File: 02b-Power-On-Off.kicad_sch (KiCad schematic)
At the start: 13 parts, among them Q1 DMG2305UX-7, Q2 DMG2305UX-7, Q4 BSS138, SW5 SW_Push

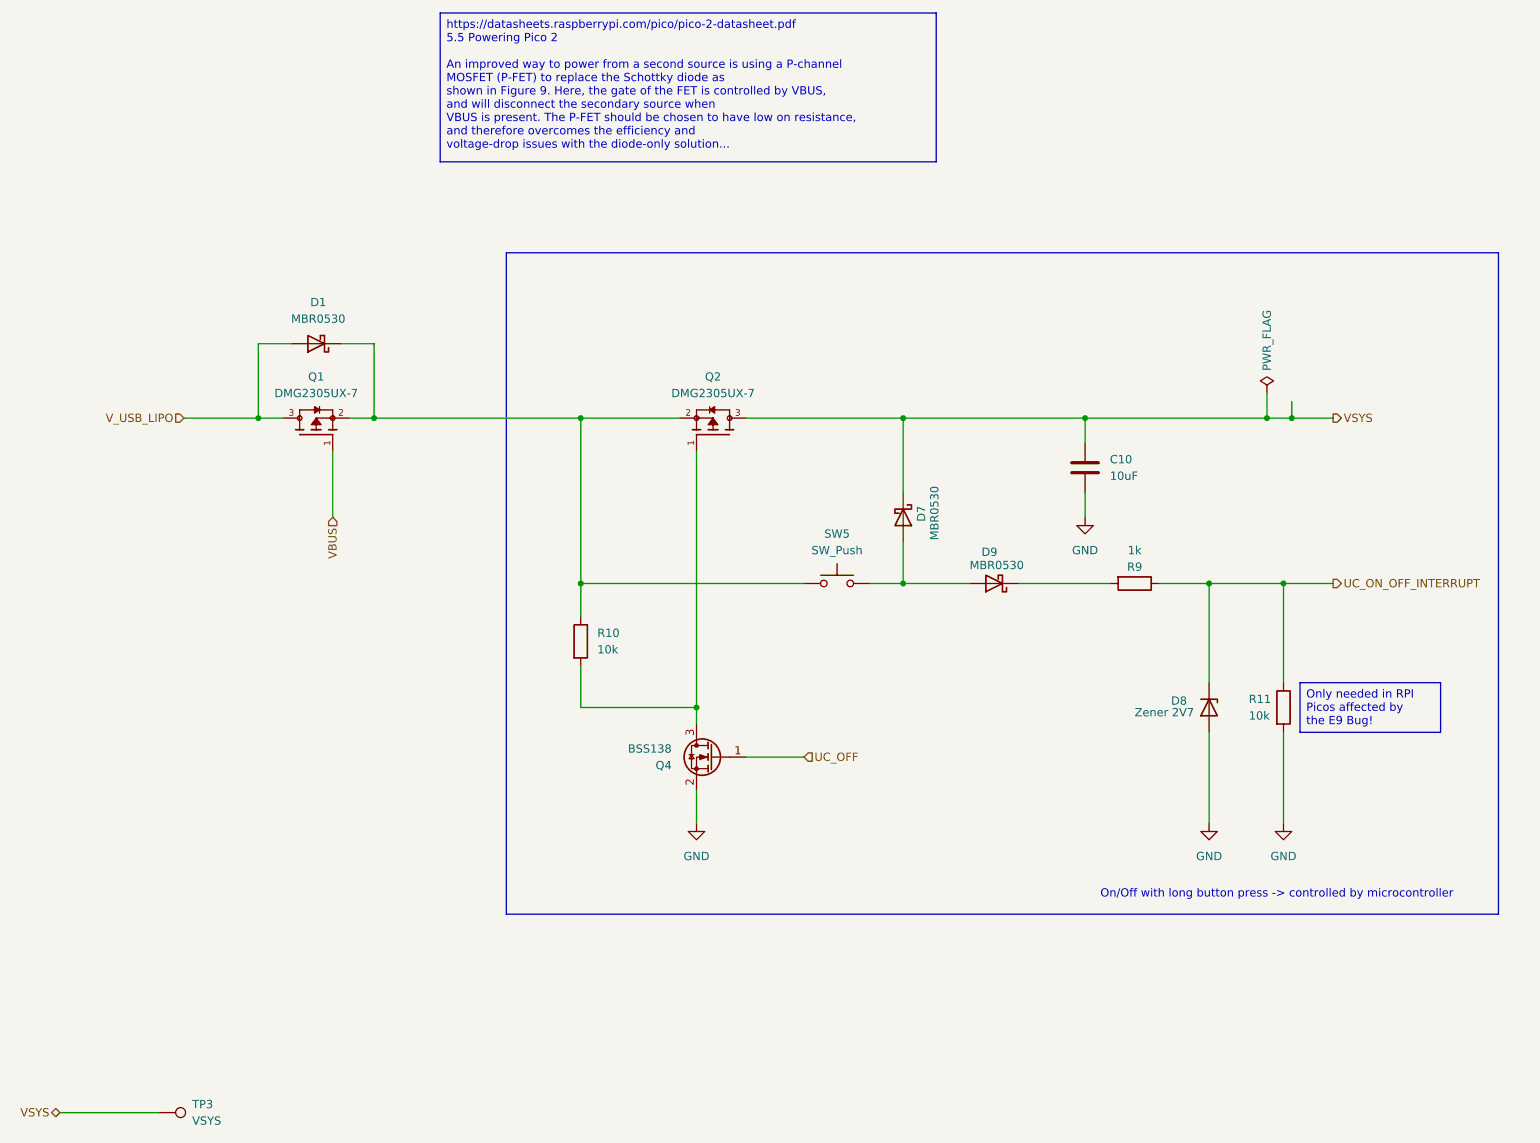
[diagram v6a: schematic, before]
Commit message: Connect both USB data lines again, checked everything with datasheets again
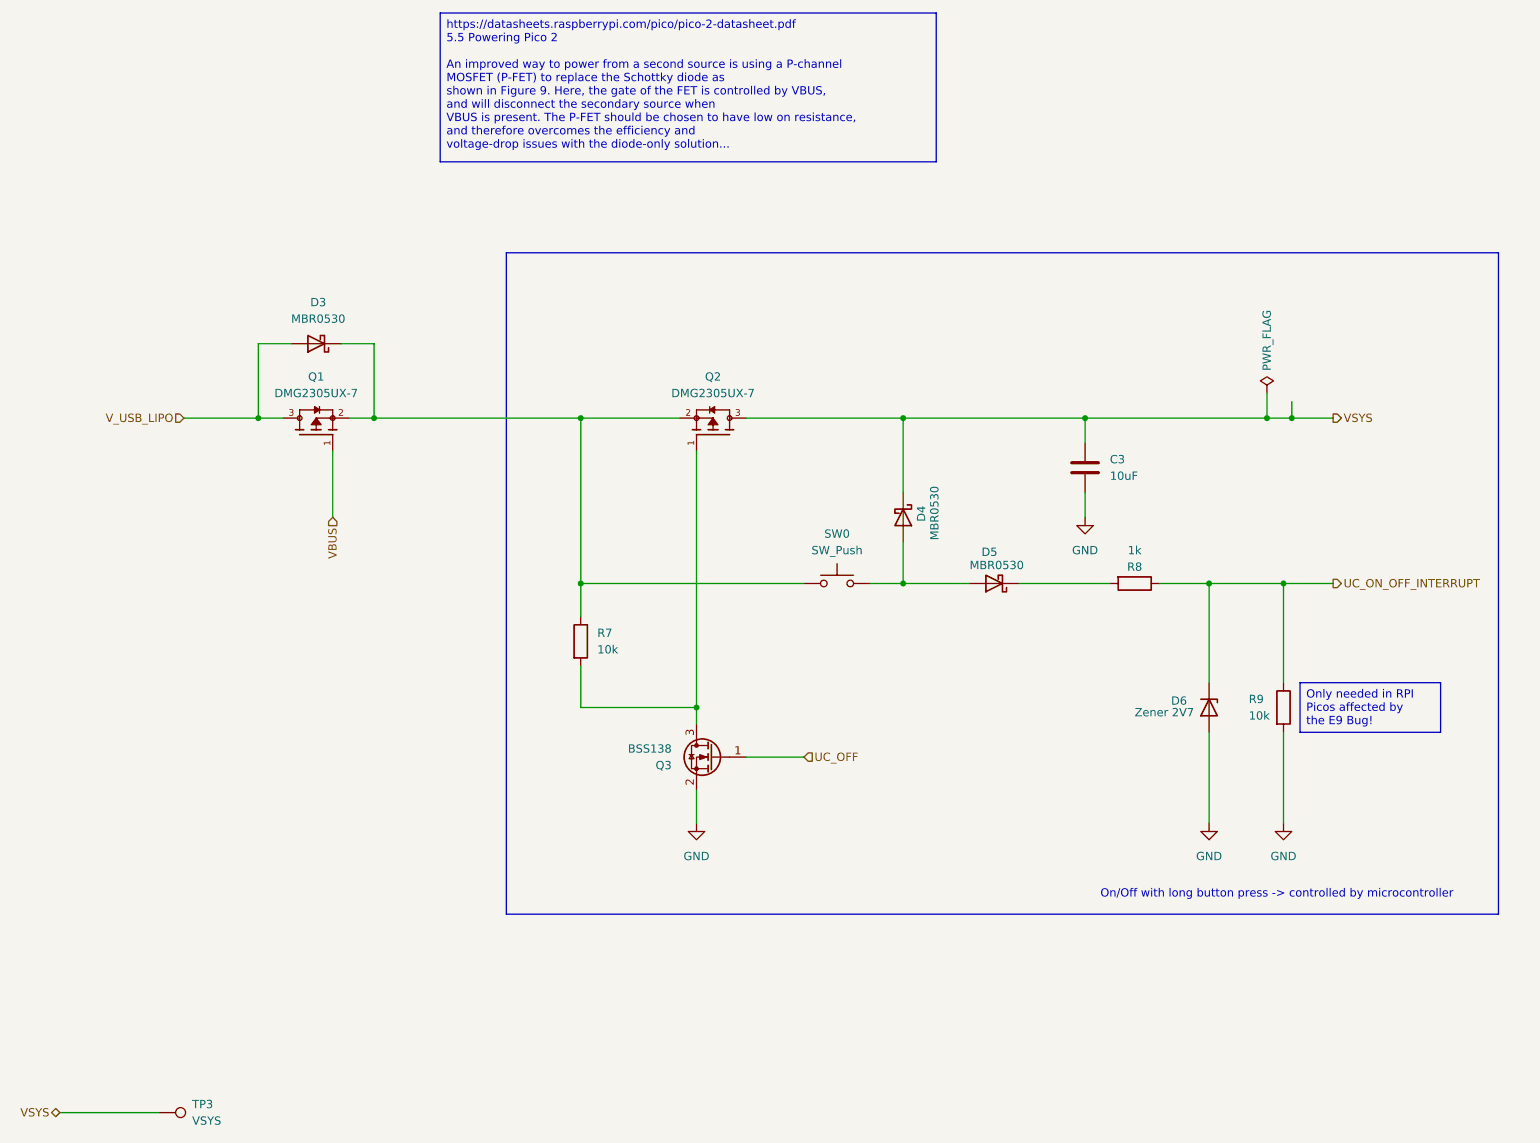
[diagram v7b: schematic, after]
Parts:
- renumbered C10 to C3, D1 to D3, D7 to D4, D9 to D5, D8 to D6, Q4 to Q3, R10 to R7, R9 to R8, R11 to R9, SW5 to SW0
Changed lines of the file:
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@@
 		(on_board yes)
 		(dnp no)
-		(property "Reference" "#PWR021"
+		(property "Reference" "#PWR015"
 			(at 190.5 97.79 0)
 			(effects
@@
 			(project "ZEReader-Pico"
 				(path "/ec954637-2a8b-4662-b4a1-f88107f11cb0/a3bedda0-cdd4-4cf1-8725-53db0608a498"
-					(reference "#PWR021")
+					(reference "#PWR015")
 					(unit 1)
 				)
@@
 		(on_board yes)
 		(dnp no)
-		(property "Reference" "R11"
+		(property "Reference" "R9"
 			(at 215.646 119.38 0)
 			(effects
@@
 			(project ""
 				(path "/ec954637-2a8b-4662-b4a1-f88107f11cb0/a3bedda0-cdd4-4cf1-8725-53db0608a498"
-					(reference "R11")
+					(reference "R9")
 					(unit 1)
 				)
@@
 		(on_board yes)
 		(dnp no)
-		(property "Reference" "D9"
+		(property "Reference" "D5"
 			(at 177.038 96.774 0)
 			(effects
@@
 			(project "ZEReader-Pico"
 				(path "/ec954637-2a8b-4662-b4a1-f88107f11cb0/a3bedda0-cdd4-4cf1-8725-53db0608a498"
-					(reference "D9")
+					(reference "D5")
 					(unit 1)
 				)
@@
 		(dnp no)
 		(fields_autoplaced yes)
-		(property "Reference" "R10"
+		(property "Reference" "R7"
 			(at 115.57 109.2199 0)
 			(effects
@@
 			(project ""
 				(path "/ec954637-2a8b-4662-b4a1-f88107f11cb0/a3bedda0-cdd4-4cf1-8725-53db0608a498"
-					(reference "R10")
+					(reference "R7")
 					(unit 1)
 				)
@@
 		(on_board yes)
 		(dnp no)
-		(property "Reference" "D7"
+		(property "Reference" "D4"
 			(at 165.354 89.662 0)
 			(effects
@@
 			(project "ZEReader-Pico"
 				(path "/ec954637-2a8b-4662-b4a1-f88107f11cb0/a3bedda0-cdd4-4cf1-8725-53db0608a498"
-					(reference "D7")
+					(reference "D4")
 					(unit 1)
 				)
@@
 		(on_board yes)
 		(dnp no)
-		(property "Reference" "#FLG06"
+		(property "Reference" "#FLG03"
 			(at 218.44 70.485 0)
 			(effects
@@
 			(project "ZEReader-Pico"
 				(path "/ec954637-2a8b-4662-b4a1-f88107f11cb0/a3bedda0-cdd4-4cf1-8725-53db0608a498"
-					(reference "#FLG06")
+					(reference "#FLG03")
 					(unit 1)
 				)
@@
 		(on_board yes)
 		(dnp no)
-		(property "Reference" "Q4"
+		(property "Reference" "Q3"
 			(at 127 129.5401 0)
 			(effects
@@
 			(project "ZEReader-Pico"
 				(path "/ec954637-2a8b-4662-b4a1-f88107f11cb0/a3bedda0-cdd4-4cf1-8725-53db0608a498"
-					(reference "Q4")
+					(reference "Q3")
 					(unit 1)
 				)
@@
 		(on_board yes)
 		(dnp no)
-		(property "Reference" "C10"
+		(property "Reference" "C3"
 			(at 194.31 82.5499 0)
 			(effects
@@
 			(project "ZEReader-Pico"
 				(path "/ec954637-2a8b-4662-b4a1-f88107f11cb0/a3bedda0-cdd4-4cf1-8725-53db0608a498"
-					(reference "C10")
+					(reference "C3")
 					(unit 1)
 				)
@@
 		(dnp no)
 		(fields_autoplaced yes)
-		(property "Reference" "#PWR023"
+		(property "Reference" "#PWR016"
 			(at 209.55 144.78 0)
 			(effects
@@
 			(project "ZEReader-Pico"
 				(path "/ec954637-2a8b-4662-b4a1-f88107f11cb0/a3bedda0-cdd4-4cf1-8725-53db0608a498"
-					(reference "#PWR023")
+					(reference "#PWR016")
 					(unit 1)
 				)
@@
 		(on_board yes)
 		(dnp no)
-		(property "Reference" "R9"
+		(property "Reference" "R8"
 			(at 198.12 99.06 90)
 			(effects
@@
 			(project ""
 				(path "/ec954637-2a8b-4662-b4a1-f88107f11cb0/a3bedda0-cdd4-4cf1-8725-53db0608a498"
-					(reference "R9")
+					(reference "R8")
 					(unit 1)
 				)
@@
 		(dnp no)
 		(fields_autoplaced yes)
-		(property "Reference" "#PWR020"
+		(property "Reference" "#PWR014"
 			(at 130.81 144.78 0)
 			(effects
@@
 			(project ""
 				(path "/ec954637-2a8b-4662-b4a1-f88107f11cb0/a3bedda0-cdd4-4cf1-8725-53db0608a498"
-					(reference "#PWR020")
+					(reference "#PWR014")
 					(unit 1)
 				)
@@
 		(dnp no)
 		(fields_autoplaced yes)
-		(property "Reference" "D1"
+		(property "Reference" "D3"
 			(at 72.7075 58.42 0)
 			(effects
@@
 			(project "ZEReader-Pico"
 				(path "/ec954637-2a8b-4662-b4a1-f88107f11cb0/a3bedda0-cdd4-4cf1-8725-53db0608a498"
-					(reference "D1")
+					(reference "D3")
 					(unit 1)
 				)
@@
 		(dnp no)
 		(fields_autoplaced yes)
-		(property "Reference" "#PWR019"
+		(property "Reference" "#PWR017"
 			(at 220.98 144.78 0)
 			(effects
@@
 			(project ""
 				(path "/ec954637-2a8b-4662-b4a1-f88107f11cb0/a3bedda0-cdd4-4cf1-8725-53db0608a498"
-					(reference "#PWR019")
+					(reference "#PWR017")
 					(unit 1)
 				)
@@
 		(dnp no)
 		(fields_autoplaced yes)
-		(property "Reference" "SW5"
+		(property "Reference" "SW0"
 			(at 152.4 93.98 0)
 			(effects
@@
 			(project "ZEReader-Pico"
 				(path "/ec954637-2a8b-4662-b4a1-f88107f11cb0/a3bedda0-cdd4-4cf1-8725-53db0608a498"
-					(reference "SW5")
+					(reference "SW0")
 					(unit 1)
 				)
@@
 		(on_board yes)
 		(dnp no)
-		(property "Reference" "D8"
+		(property "Reference" "D6"
 			(at 203.708 119.634 90)
 			(effects
@@
 			(project ""
 				(path "/ec954637-2a8b-4662-b4a1-f88107f11cb0/a3bedda0-cdd4-4cf1-8725-53db0608a498"
-					(reference "D8")
-					(unit 1)
-				)
+					(reference "D6")
+					(unit 1)
+				)
